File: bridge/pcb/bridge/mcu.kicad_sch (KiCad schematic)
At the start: 28 parts, among them J5 Conn_01x04, J6 Conn_01x02, J7 Conn_01x03, J8 Conn_01x02, J9 MCU_Test_Point, SW2 SW_SPST, SW3 SW_SPST, SW4 SW_SPST, U1 L293, U4 ATmega328P-P, U5 L7805, U6 MCP4901

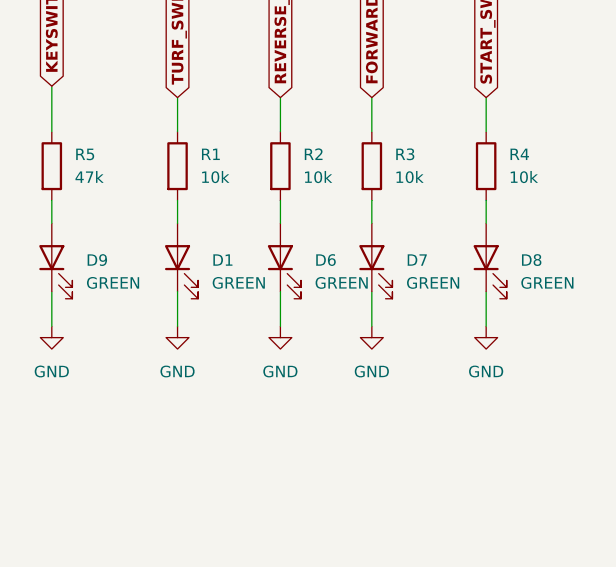
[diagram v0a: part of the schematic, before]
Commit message: Adjusted LED colors
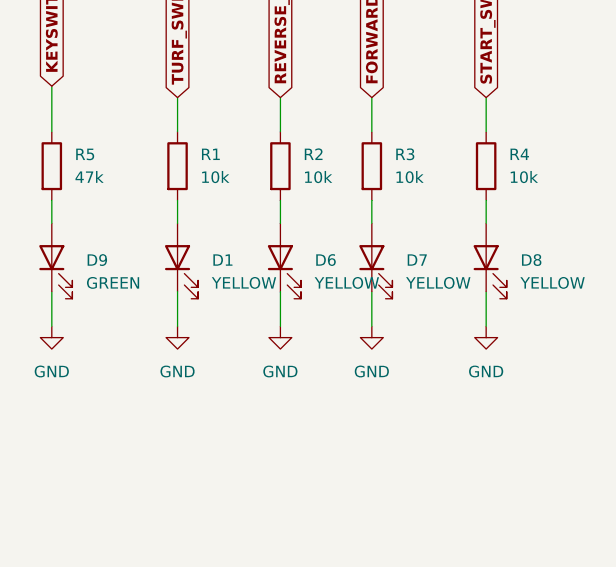
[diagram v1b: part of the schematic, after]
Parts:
- D1, D6, D7, D8: value GREEN -> YELLOW
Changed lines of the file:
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@@
       (effects (font (size 1.27 1.27)) (justify right))
     )
-    (property "Value" "GREEN" (at 259.08 146.3675 90)
+    (property "Value" "YELLOW" (at 259.08 146.3675 90)
       (effects (font (size 1.27 1.27)) (justify right))
     )
@@
       (effects (font (size 1.27 1.27)) (justify right))
     )
-    (property "Value" "GREEN" (at 271.78 146.3675 90)
+    (property "Value" "YELLOW" (at 271.78 146.3675 90)
       (effects (font (size 1.27 1.27)) (justify right))
     )
@@
       (effects (font (size 1.27 1.27)) (justify right))
     )
-    (property "Value" "GREEN" (at 237.49 146.3675 90)
+    (property "Value" "YELLOW" (at 237.49 146.3675 90)
       (effects (font (size 1.27 1.27)) (justify right))
     )
@@
       (effects (font (size 1.27 1.27)) (justify right))
     )
-    (property "Value" "GREEN" (at 248.92 146.3675 90)
+    (property "Value" "YELLOW" (at 248.92 146.3675 90)
       (effects (font (size 1.27 1.27)) (justify right))
     )
